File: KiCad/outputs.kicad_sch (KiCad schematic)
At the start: 39 parts, among them J1 UART, J10 LED2, J13 LED3, J14 LED4, J15 LED8, J16 LED7, J17 LED6, J18 LED5, J19 LED9, J20 LED10, J21 LED11, J22 LED12, J4 5V, J5 24V, J6 USB_C_Receptacle_USB2.0_16P, J7 Conn_01x14, J8 JTAG, J9 LED1, U7 SN74LVC8T245, U8 SN74LVC8T245

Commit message: arrange  components
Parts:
- removed J21: LED11, CONN-TH_3P-P5.08_WJ2EDGRC-5.08-3P, symbol Connector_Generic:Conn_01x03
- removed J22: LED12, CONN-TH_3P-P5.08_WJ2EDGRC-5.08-3P, symbol Connector_Generic:Conn_01x03
- removed R45, R46: 100, Resistor_SMD:R_0805_2012Metric_Pad1.20x1.40mm_HandSolder, symbol Device:R_Small
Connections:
- net Data12 is gone; now on net Data10: U8.6 (A4)
- net Data1: now also U7.10 (A8); no longer U7.3 (A1)
- net Data10: no longer U8.4 (A2)
- net Data2: now also U7.9 (A7); no longer U7.4 (A2)
- net Data3: now also U7.8 (A6); no longer U7.5 (A3)
- net Data4: now also U7.7 (A5); no longer U7.6 (A4)
- net Data5: now also U7.6 (A4); no longer U7.7 (A5)
- net Data6: now also U8.10 (A8); no longer U7.8 (A6)
- net Data7: now also U8.9 (A7); no longer U7.9 (A7)
- net Data8: now also U8.8 (A6); no longer U7.10 (A8)
- net Data9: now also U8.7 (A5); no longer U8.3 (A1)
- net DataOut1: now also R42.2; no longer R35.2
- net DataOut2: now also R41.2; no longer R36.2
- net DataOut3: now also R40.2; no longer R37.2
- net DataOut4: now also R39.2; no longer R38.2
- net DataOut5: now also R38.2; no longer R39.2
- net DataOut6: now also R37.2; no longer R40.2
- net DataOut7: now also R36.2; no longer R41.2
- net DataOut8: now also R35.2; no longer R42.2
- net at R35.1: now also U8.16 (B6); no longer U7.21 (B1)
- net at U7.20 (B2): no longer R36.1
- net at U8.18 (B4): now also R44.1
- net at U7.19 (B3): no longer R37.1
- net at R43.1: now also U8.17 (B5); no longer U8.21 (B1)
- net at U8.20 (B2): no longer R44.1
- net at U8.14 (B8): now also R37.1
- net at U8.15 (B7): now also R36.1
- net Data11: no longer names the net of U8.5 (A3)
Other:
- note added: "Jumper für power over usb, zusätzlich eine ideale Diode"
- note removed: "Idee: Seperate connector für 12-24V input und 5V input. Beim 5V input wird der 5V Buck converter gebypassed"

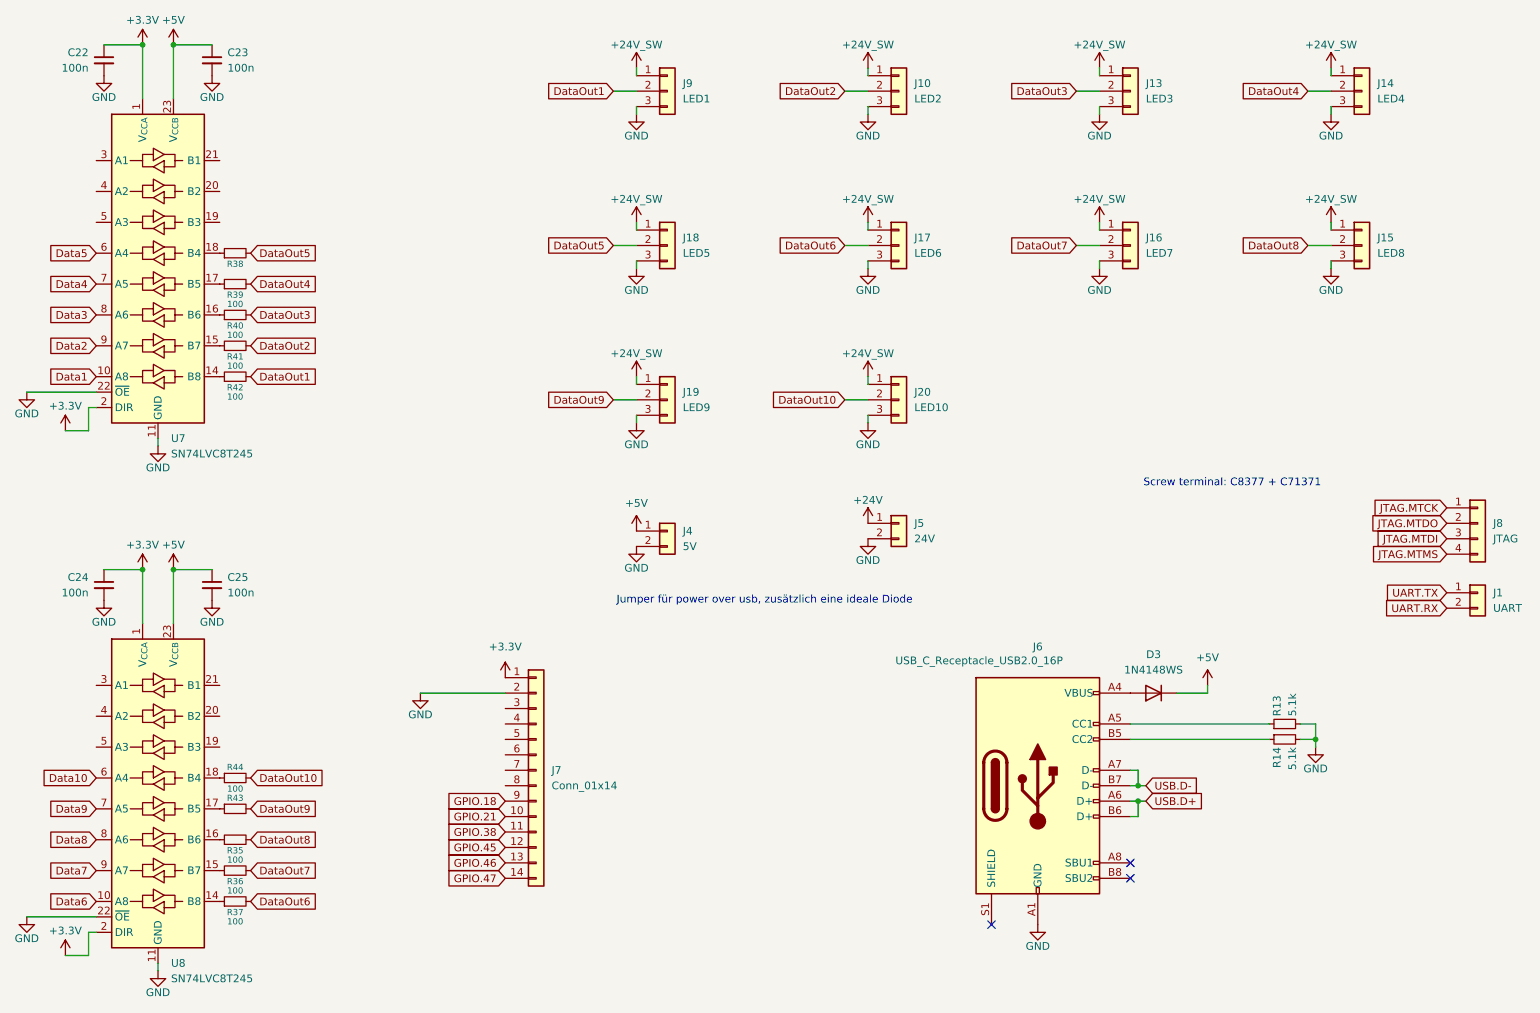
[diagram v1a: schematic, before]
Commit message: add ideal diode
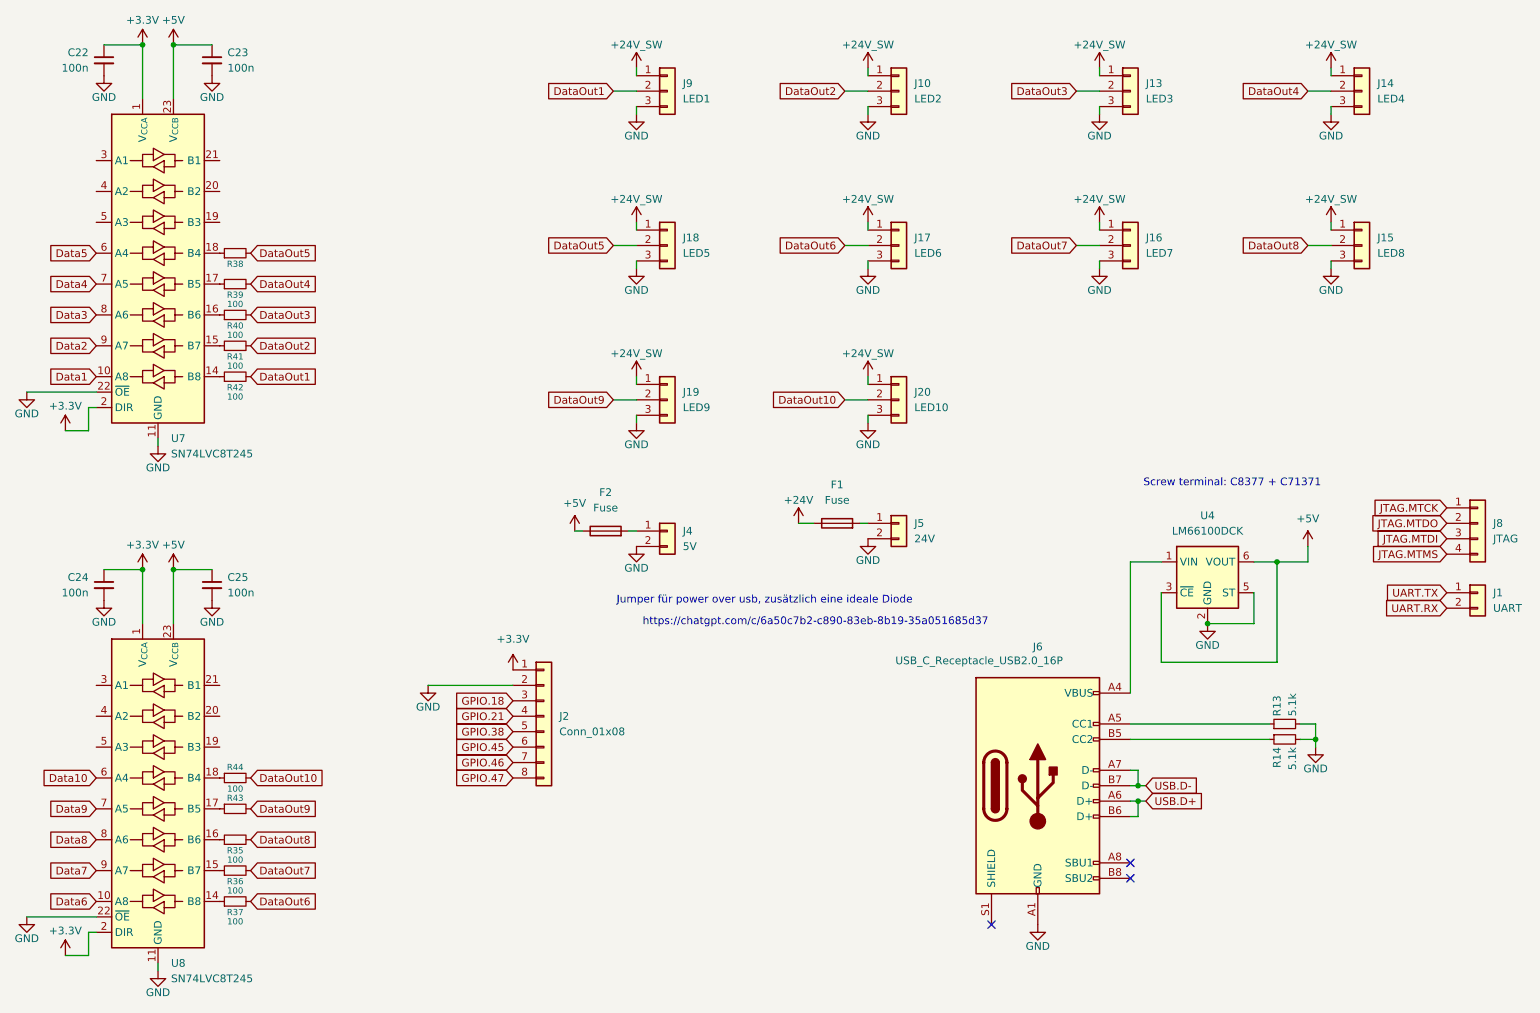
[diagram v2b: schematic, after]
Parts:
- removed D3: 1N4148WS, Diode_SMD:D_SOD-323, symbol Diode:1N4148WS
- removed J7: Conn_01x14, Connector_PinHeader_2.54mm:PinHeader_1x14_P2.54mm_Vertical, symbol Connector_Generic:Conn_01x14
- added F1, F2: Fuse, Fuse:Fuseholder_Blade_Mini_Keystone_3568, symbol Device:Fuse
- added J2: Conn_01x08, Connector_PinHeader_2.54mm:PinHeader_1x08_P2.54mm_Vertical, symbol Connector_Generic:Conn_01x08
- added U4: LM66100DCK, Package_TO_SOT_SMD:SOT-363_SC-70-6, symbol Power_Management:LM66100DCK
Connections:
- net +24V: now also F1.1; no longer J5.1 (Pin_1)
- net +3.3V: now also J2.1 (Pin_1)
- net +5V: now also F2.1, U4.3 (~{CE}), U4.6 (VOUT); no longer J4.1 (Pin_1)
- net GND: now also J2.2 (Pin_2), U4.2 (GND), U4.5 (ST)
- net GPIO.18: now also J2.3 (Pin_3)
- net GPIO.21: now also J2.4 (Pin_4)
- net GPIO.38: now also J2.5 (Pin_5)
- net GPIO.45: now also J2.6 (Pin_6)
- net GPIO.46: now also J2.7 (Pin_7)
- net GPIO.47: now also J2.8 (Pin_8)
- net at J6.A4 (VBUS), J6.A9 (VBUS), J6.B4 (VBUS)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: now also U4.1 (VIN)
- new net: F2.2, J4.1 (Pin_1)
- new net: F1.2, J5.1 (Pin_1)
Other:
- note added: "https://chatgpt.com/c/6a50c7b2-c890-83eb-8b19-35a051685d37"

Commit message: add esd protection, pullup on EN, Replicate layout
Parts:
- added J3: Power over USB, Connector_PinHeader_2.54mm:PinHeader_1x02_P2.54mm_Vertical, symbol Connector_Generic:Conn_01x02
- added U5: USBLC6-2SC6, Package_TO_SOT_SMD:SOT-23-6, symbol Power_Protection:USBLC6-2SC6
- U4: LCSC (none) -> C2869734
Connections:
- net +5V: now also J3.2 (Pin_2)
- net Data10: now also U8.3 (A1); no longer U8.6 (A4)
- net Data3: now also U7.7 (A5); no longer U7.8 (A6)
- net Data4: now also U7.5 (A3); no longer U7.7 (A5)
- net Data5: now also U7.3 (A1); no longer U7.6 (A4)
- net Data7: now also U8.8 (A6); no longer U8.9 (A7)
- net Data8: now also U8.6 (A4); no longer U8.8 (A6)
- net Data9: now also U8.4 (A2); no longer U8.7 (A5)
- net GND: now also R13.1, R14.1, U5.2 (GND); no longer R13.2, R14.2
- net USB.D+: now also U5.4 (I/O2); no longer J6.A6 (D+), J6.B6 (D+)
- net USB.D-: now also U5.6 (I/O1); no longer J6.A7 (D-), J6.B7 (D-)
- net at J6.B5 (CC2): now also R13.2; no longer R14.1
- net at J6.A4 (VBUS), J6.A9 (VBUS), J6.B4 (VBUS)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: now also U5.5 (VBUS)
- net at J6.A5 (CC1): now also R14.2; no longer R13.1
- net at U7.18 (B4): no longer R38.1
- net at R35.1: now also U8.18 (B4); no longer U8.16 (B6)
- net at R43.1: now also U8.20 (B2); no longer U8.17 (B5)
- net at U7.16 (B6): no longer R40.1
- net at R39.1: now also U7.19 (B3); no longer U7.17 (B5)
- net at U7.21 (B1): now also R38.1
- net at R44.1: now also U8.21 (B1); no longer U8.18 (B4)
- net at R36.1: now also U8.16 (B6); no longer U8.15 (B7)
- net +24V renamed VCC_IN
- net VCC_IN: now also J3.1 (Pin_1)
- net +24V_SW renamed VCC_SW
- new net: J6.A7 (D-), J6.B7 (D-), U5.1 (I/O1)
- new net: J6.A6 (D+), J6.B6 (D+), U5.3 (I/O2)
- new net: R40.1, U7.17 (B5)
- no-connect marks 3 -> 15

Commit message: prepare tvs diodes
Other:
- note added: "TVS diode fehlt noch"
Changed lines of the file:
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@@
 	(generator_version "10.0")
 	(paper "A4")
+	(text "TVS diode fehlt noch"
+		(exclude_from_sim no)
+		(at 145.796 100.33 0)
+		(effects
+			(font
+				(size 1.27 1.27)
+			)
+		)
+	)
 	(text "https://chatgpt.com/c/6a50c7b2-c890-83eb-8b19-35a051685d37"
 		(exclude_from_sim no)
@@
 	(wire
 		(pts
-			(xy 149.86 96.52) (xy 152.4 96.52)
+			(xy 143.51 96.52) (xy 152.4 96.52)
 		)
 		(stroke
@@
 	(symbol
 		(lib_id "power:+3.3V")
-		(at 149.86 96.52 0)
+		(at 143.51 96.52 0)
 		(unit 1)
 		(body_style 1)
@@
 		(dnp no)
 		(property "Reference" "#PWR09"
-			(at 149.86 100.33 0)
+			(at 143.51 100.33 0)
 			(hide yes)
 			(show_name no)
@@
 		)
 		(property "Value" "VCC_IN"
-			(at 149.86 92.71 0)
+			(at 143.51 92.71 0)
 			(show_name no)
 			(do_not_autoplace no)
@@
 		)
 		(property "Footprint" ""
-			(at 149.86 96.52 0)
+			(at 143.51 96.52 0)
 			(hide yes)
 			(show_name no)
@@
 		)
 		(property "Datasheet" ""
-			(at 149.86 96.52 0)
+			(at 143.51 96.52 0)
 			(hide yes)
 			(show_name no)
@@
 		)
 		(property "Description" "Power symbol creates a global label with name \"+3.3V\""
-			(at 149.86 96.52 0)
+			(at 143.51 96.52 0)
 			(hide yes)
 			(show_name no)
